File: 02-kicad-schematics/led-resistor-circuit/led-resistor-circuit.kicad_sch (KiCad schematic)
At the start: 3 parts

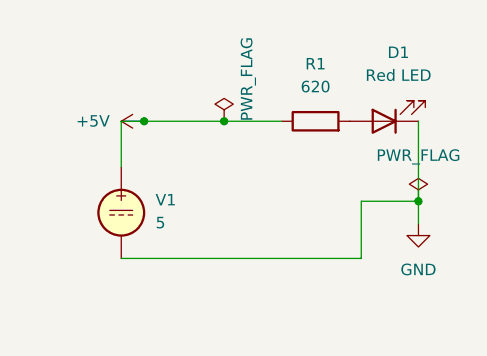
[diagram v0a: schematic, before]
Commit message: Add LED resistor circuit and SPICE simulation
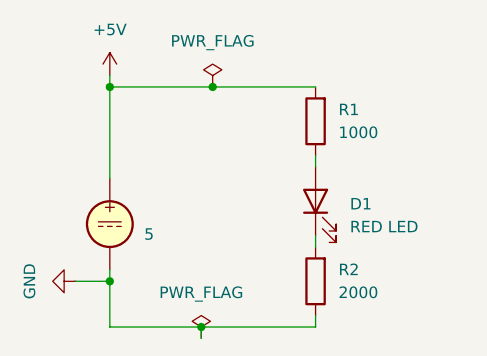
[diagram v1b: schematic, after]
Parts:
- added R2: 2000, symbol Device:R
- D1: value Red LED -> RED LED
- R1: value 620 -> 1000
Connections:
- net +5V: now also R1.2; no longer R1.1
- net GND: now also R2.1; no longer D1.1 (K)
- net at D1.2 (A): now also R1.1; no longer R1.2
- new net: D1.1 (K), R2.2
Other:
- moved on the sheet: R1
